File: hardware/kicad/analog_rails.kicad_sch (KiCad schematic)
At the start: 35 parts, among them U401 LMR62014XMF, U402 LT3042EMSE, U403 LM27761DSG, U404 REF5025AID

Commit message: feat(hardware)!: draw draft A1 of the schematic around a Pico 2
A Raspberry Pi Pico 2 on two 1x20 sockets replaces the ESP32-S3
development board, the programmable logic device and the buffer
between the two boards (D-39 to D-43 of the specification). The former
interface and range logic sheets become two new ones:

- Controller: the Pico 2, the diodes that join its USB supply and the
  5 V rail of the carrier, resistor arrays in the SPI and acquisition
  lines, a reset button and a console header.
- Side Data: two shift registers that take the range, the status
  signals and the eight logic inputs with every sample.

The DUT connects through a 1x4 pin header and a lever terminal block
in parallel, both GND, VIN, VOUT, GND, and the logic port is a 1x10
header with VCC, GND, D7 to D0: the pin order of the PPK2 (D-44). A
solder jumper selects the supply of the DUT side of the level
translator. A transistor at the driver of the ampere switch holds it
open while VIN is above 5.5 V.

Reference designators are numbered as the annotation tool of KiCad
does by default (D-45). The numbering touches every sheet, so these
changes come in one commit. The symbol and the socket footprint of
the ESP32-S3 board leave the project library; the Pico 2 uses the
symbol and the footprint of the KiCad library.

The electrical rules check reports no errors and no warnings. The
parts stay candidates, and no program for the PIO blocks exists yet.

BREAKING CHANGE: the pins of the controller follow the new pin map of
section 5 of the specification.
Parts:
- renumbered C402 to C10, C408 to C11, C409 to C12, C410 to C13, C411 to C14, C401 to C15, C403 to C16, C404 to C17, C405 to C18, C412 to C19, C407 to C20, C414 to C21, C413 to C22, C406 to C23, D401 to D5, L401 to L1, R410 to R10, R404 to R11, R405 to R12, R407 to R13, R406 to R14, R408 to R5, R401 to R6, R402 to R7, R403 to R8, R409 to R9, TP402 to TP10, TP403 to TP6, TP401 to TP7, TP405 to TP8, TP404 to TP9, U401 to U4, U403 to U5, U404 to U6, U402 to U7
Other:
- note added: "U4: VOUT = 1.23 V x (1 + R7 / R8) = 13.5 V, 1.6 MHz. U7: VOUT = 100 uA x R11 = 12.0 V; PG opens above 11 V (R12, R14). U5: VOUT = -1.22 V x (R9 + R10) / R10 = -3.98 V; R5 keeps VBUS transients off its 5.8 V rating. PWR_GOOD is pulled up to +3V3_C: with the carrier unpowered it reads low."
- note removed: "U401: VOUT = 1.23 V x (1 + R402 / R403) = 13.5 V, 1.6 MHz. U402: VOUT = 100 uA x R404 = 12.0 V; PG opens above 11 V (R405, R406). U403: VOUT = -1.22 V x (R409 + R410) / R410 = -3.98 V; R408 keeps VBUS transients off its 5.8 V rating. PWR_GOOD is pulled up to +3V3_C: with the carrier unpowered it reads low."

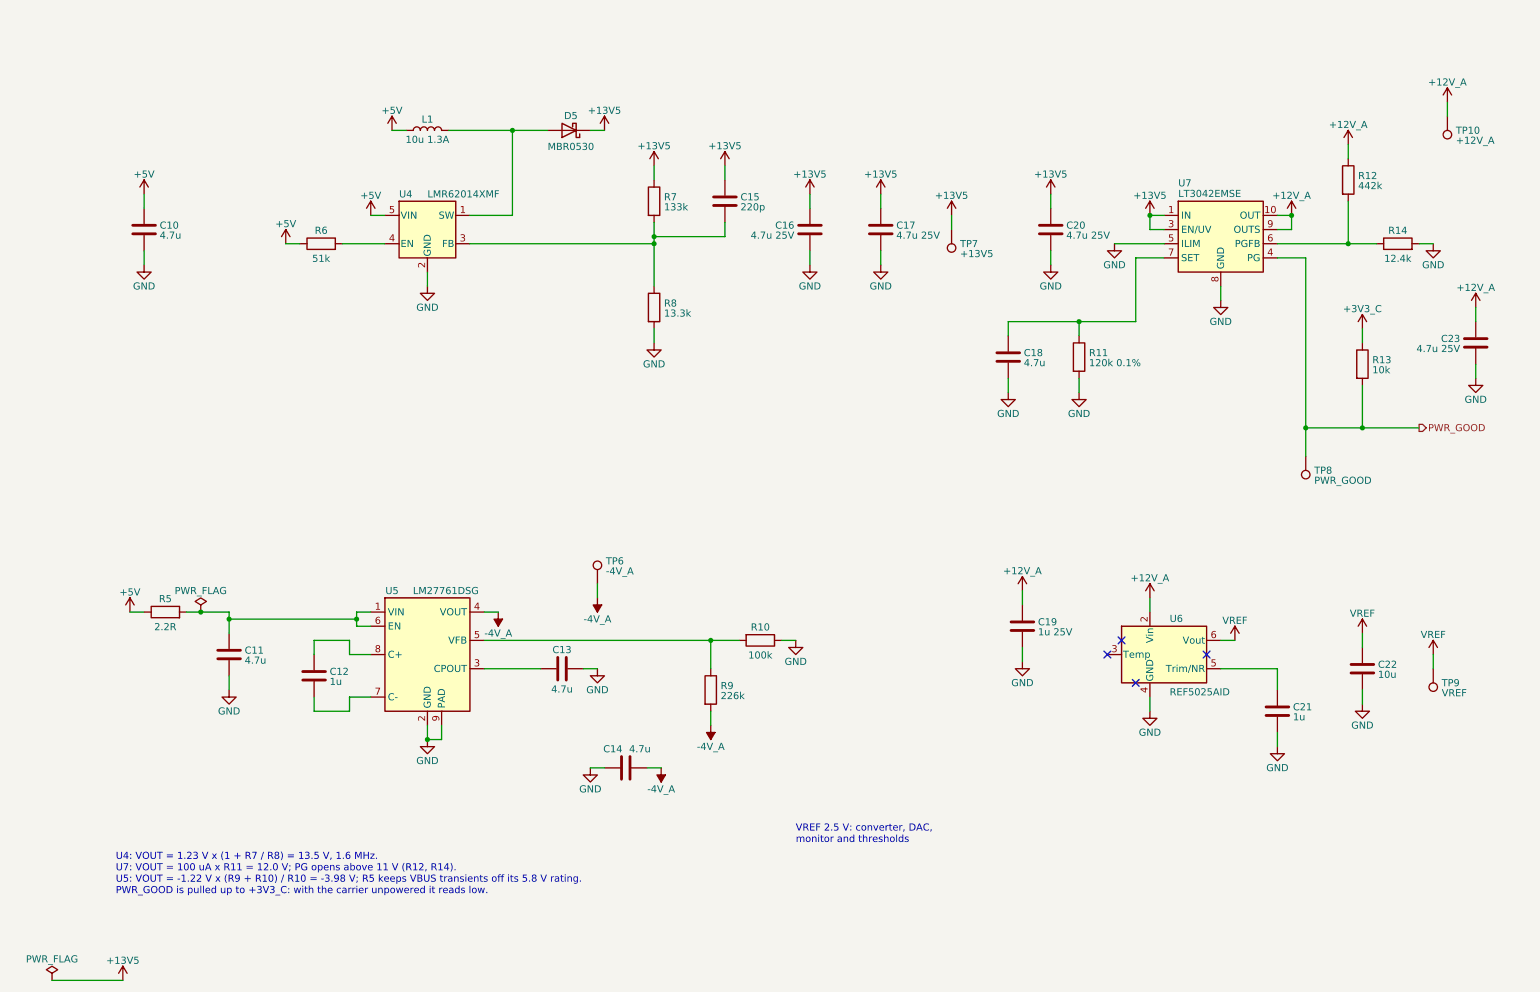
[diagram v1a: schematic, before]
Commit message: feat(hardware): draw draft A2 of the schematic
428 parts on 15 A4 pages, 14 sheets below the root sheet (D-83). Two
sheets are new: Logic Supplies, with the supervisor of the 5 V rail and
the two 3.3 V regulators, and Rail Monitor, with the comparators behind
PWR_GOOD.

The drawings follow the specification of draft A2: a current limiter
on each supply input and a priority multiplexer, a pre-regulator that
tracks the output of the linear regulator, a VIN path that withstands
-20 V to +20 V with its switch open, two diode-connected MOSFETs as
ladder clamp, thin-film and four-terminal shunts, ESD arrays at the CC
pins and at the VCC pin of the logic port. The reference designators
are numbered as KiCad numbers them (D-45), so they are not those of
draft A1.

The project library gains the symbol of the input multiplexer and two
footprints: the lever terminal block with pads of 1.9 mm x 2.3 mm and
the controller module without its antenna keep-out (D-85).

The electrical rules check reports no errors and no warnings. The
parts are candidates, and nothing is built or measured.
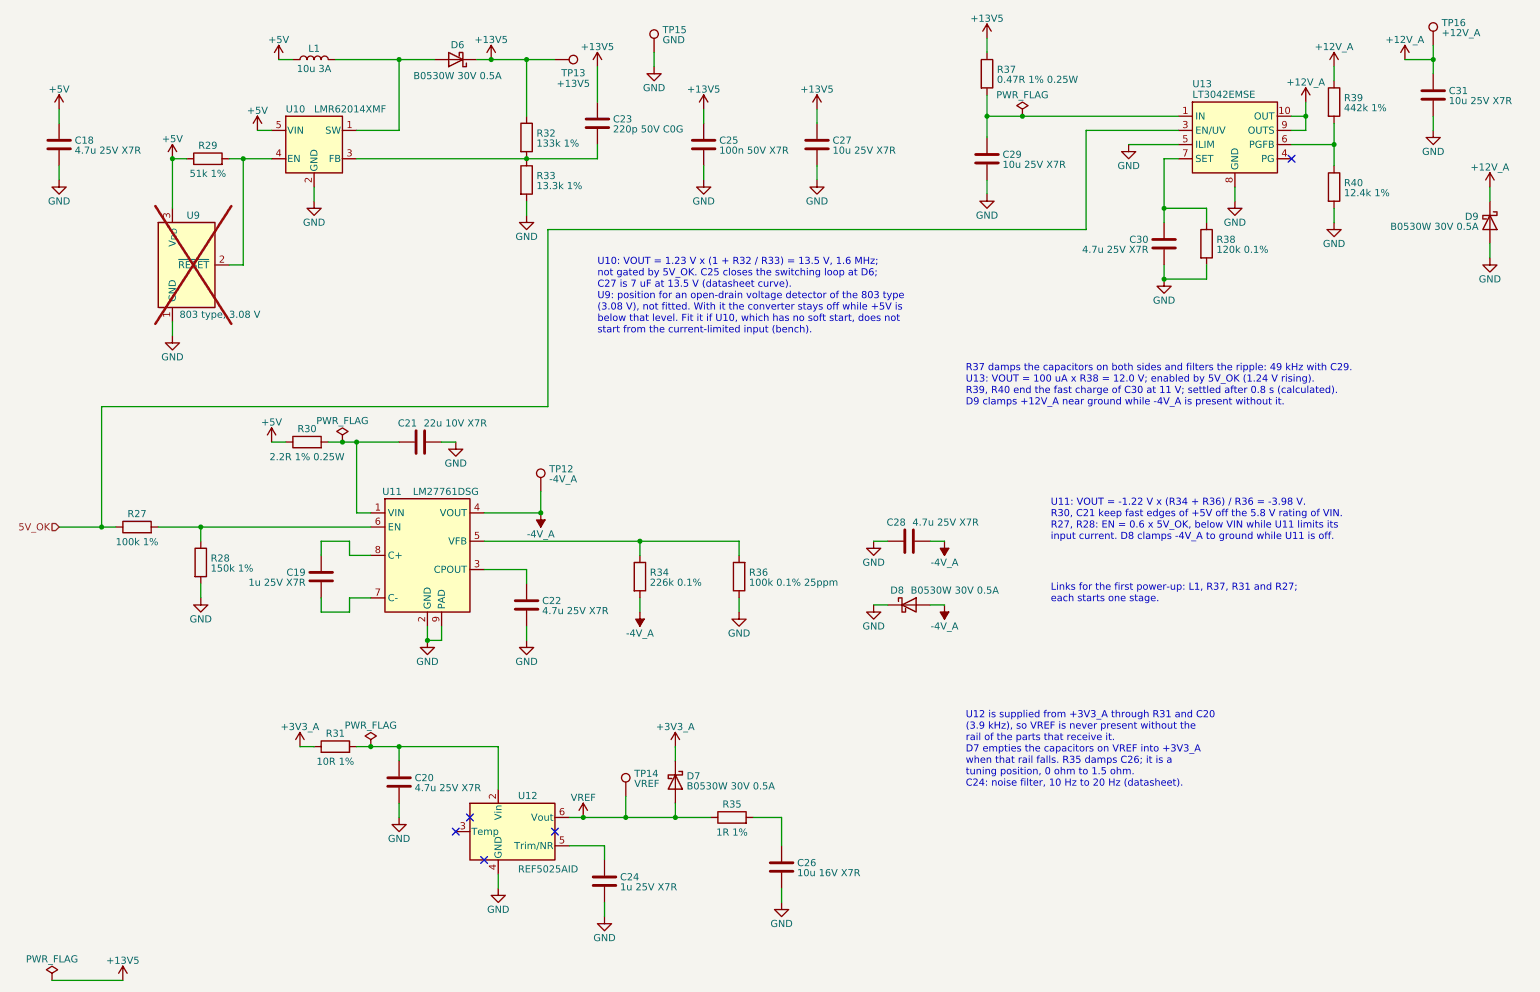
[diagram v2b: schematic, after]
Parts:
- removed R13: 10k, Resistor_SMD:R_0603_1608Metric, symbol Device:R
- removed TP8: PWR_GOOD, TestPoint:TestPoint_Pad_D1.5mm, symbol Connector:TestPoint
- added D7, D8, D9: B0530W 30V 0.5A, Diode_SMD:D_SOD-123, symbol Device:D_Schottky
- added R27: 100k 1%, Resistor_SMD:R_0603_1608Metric, symbol Device:R
- added R28: 150k 1%, Resistor_SMD:R_0603_1608Metric, symbol Device:R
- added R31: 10R 1%, Resistor_SMD:R_0603_1608Metric, symbol Device:R
- added R35: 1R 1%, Resistor_SMD:R_0603_1608Metric, symbol Device:R
- added R37: 0.47R 1% 0.25W, Resistor_SMD:R_1206_3216Metric, symbol Device:R
- added TP15: GND, TestPoint:TestPoint_Pad_2.0x2.0mm, symbol Connector:TestPoint
- added U9: 803 type, 3.08 V, Package_TO_SOT_SMD:SOT-23, symbol Power_Supervisor:TCM809
- C18: renamed from C10; value 4.7u -> 4.7u 25V X7R; MPN (none) -> CL21B475KAFNNNE; Manufacturer (none) -> Samsung Electro-Mechanics
- C19: renamed from C12; value 1u -> 1u 25V X7R; MPN (none) -> C0603C105K3RACTU; Manufacturer (none) -> KEMET
- C20: renamed from C19; value 1u 25V -> 4.7u 25V X7R; footprint Capacitor_SMD:C_0603_1608Metric -> Capacitor_SMD:C_0805_2012Metric; MPN (none) -> CL21B475KAFNNNE; Manufacturer (none) -> Samsung Electro-Mechanics
- C21: renamed from C11; value 4.7u -> 22u 10V X7R; footprint Capacitor_SMD:C_0805_2012Metric -> Capacitor_SMD:C_1206_3216Metric; MPN (none) -> CL31B226KPHNNNE; Manufacturer (none) -> Samsung Electro-Mechanics
- C22: renamed from C13; value 4.7u -> 4.7u 25V X7R; MPN (none) -> CL21B475KAFNNNE; Manufacturer (none) -> Samsung Electro-Mechanics
- C23: renamed from C15; value 220p -> 220p 50V C0G; MPN (none) -> C0603C221J5GACTU; Manufacturer (none) -> KEMET
- C24: renamed from C21; value 1u -> 1u 25V X7R; MPN (none) -> C0603C105K3RACTU; Manufacturer (none) -> KEMET
- C25: renamed from C17; value 4.7u 25V -> 100n 50V X7R; footprint Capacitor_SMD:C_0805_2012Metric -> Capacitor_SMD:C_0603_1608Metric; MPN (none) -> C0603C104K5RACTU; Manufacturer (none) -> KEMET
- C26: renamed from C22; value 10u -> 10u 16V X7R; MPN (none) -> CL21B106KOQNNNE; Manufacturer (none) -> Samsung Electro-Mechanics
- C27: renamed from C16; value 4.7u 25V -> 10u 25V X7R; footprint Capacitor_SMD:C_0805_2012Metric -> Capacitor_SMD:C_1210_3225Metric; MPN (none) -> CL32B106KAJNNNE; Manufacturer (none) -> Samsung Electro-Mechanics
- C28: renamed from C14; value 4.7u -> 4.7u 25V X7R; MPN (none) -> CL21B475KAFNNNE; Manufacturer (none) -> Samsung Electro-Mechanics
- C29: renamed from C20; value 4.7u 25V -> 10u 25V X7R; footprint Capacitor_SMD:C_0805_2012Metric -> Capacitor_SMD:C_1210_3225Metric; MPN (none) -> CL32B106KAJNNNE; Manufacturer (none) -> Samsung Electro-Mechanics
- C30: renamed from C18; value 4.7u -> 4.7u 25V X7R; MPN (none) -> CL21B475KAFNNNE; Manufacturer (none) -> Samsung Electro-Mechanics
- C31: renamed from C23; value 4.7u 25V -> 10u 25V X7R; footprint Capacitor_SMD:C_0805_2012Metric -> Capacitor_SMD:C_1210_3225Metric; MPN (none) -> CL32B106KAJNNNE; Manufacturer (none) -> Samsung Electro-Mechanics
- D6: renamed from D5; value MBR0530 -> B0530W 30V 0.5A; MPN (none) -> B0530W-7-F; Manufacturer (none) -> Diodes Incorporated
- L1: value 10u 1.3A -> 10u 3A; footprint Inductor_SMD:L_Changjiang_FNR4020S -> Inductor_SMD:L_Wuerth_MAPI-4030; MPN FNR4020S100MT -> 74438357100; Manufacturer (none) -> Wurth Elektronik
- R29: renamed from R6; value 51k -> 51k 1%; MPN (none) -> CRCW060351K0FKEA; Manufacturer (none) -> Vishay
- R30: renamed from R5; value 2.2R -> 2.2R 1% 0.25W; footprint Resistor_SMD:R_0603_1608Metric -> Resistor_SMD:R_1206_3216Metric; MPN (none) -> CRCW12062R20FKEA; Manufacturer (none) -> Vishay
- R32: renamed from R7; value 133k -> 133k 1%; MPN (none) -> CRCW0603133KFKEA; Manufacturer (none) -> Vishay
- R33: renamed from R8; value 13.3k -> 13.3k 1%; MPN (none) -> CRCW060313K3FKEA; Manufacturer (none) -> Vishay
- R34: renamed from R9; value 226k -> 226k 0.1%; MPN (none) -> TNPW0603226KBEEA; Manufacturer (none) -> Vishay
- R36: renamed from R10; value 100k -> 100k 0.1% 25ppm; MPN (none) -> TNPW0603100KBEEA; Manufacturer (none) -> Vishay
- R38: renamed from R11; MPN (none) -> TNPW0603120KBEEA; Manufacturer (none) -> Vishay
- R39: renamed from R12; value 442k -> 442k 1%; MPN (none) -> CRCW0603442KFKEA; Manufacturer (none) -> Vishay
- R40: renamed from R14; value 12.4k -> 12.4k 1%; MPN (none) -> CRCW060312K4FKEA; Manufacturer (none) -> Vishay
- TP12: renamed from TP6; now left out of the parts list
- TP13: renamed from TP7; now left out of the parts list
- TP14: renamed from TP9; now left out of the parts list
- TP16: renamed from TP10; now left out of the parts list
- U10: renamed from U4; MPN (none) -> LMR62014XMF/NOPB; Manufacturer (none) -> Texas Instruments
- U11: renamed from U5; MPN (none) -> LM27761DSGT; Manufacturer (none) -> Texas Instruments
- U12: renamed from U6; MPN (none) -> REF5025AID; Manufacturer (none) -> Texas Instruments
- U13: renamed from U7; MPN (none) -> LT3042EMSE#PBF; Manufacturer (none) -> Analog Devices
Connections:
- net +12V_A: now also D9.1 (K); no longer C20.1, U12.2 (Vin)
- net +13V5: now also R37.1; no longer C29.1, U13.1 (IN), U13.2 (IN), U13.3 (EN/UV)
- net +5V: now also U9.3 (V_{DD})
- net -4V_A: now also D8.2 (A)
- net GND: now also D8.1 (K), D9.2 (A), R28.2, TP15.1, U9.1 (GND)
- net VREF: now also D7.2 (A), R35.1; no longer C26.1
- net at C21.1, R30.2, U11.1 (VIN): no longer U11.6 (EN)
- net at R29.2, U10.4 (EN): now also U9.2 (~{RESET})
- net PWR_GOOD: no longer names the net of U13.4 (PG)
- new net: C20.1, R31.2, U12.2 (Vin)
- new net: C26.1, R35.2
- new net: C29.1, R37.2, U13.1 (IN), U13.2 (IN)
- new net: R27.2, R28.1, U11.6 (EN)
- new net +3V3_A: D7.1 (K), R31.1
- new net 5V_OK: R27.1, U13.3 (EN/UV)
- no-connect marks 4 -> 5
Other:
- note added: "Links for the first power-up: L1, R37, R31 and R27; each starts one stage."
- note added: "R37 damps the capacitors on both sides and filters the ripple: 49 kHz with C29. U13: VOUT = 100 uA x R38 = 12.0 V; enabled by 5V_OK (1.24 V rising). R39, R40 end the fast charge of C30 at 11 V; settled after 0.8 s (calculated). D9 clamps +12V_A near ground while -4V_A is present without it."
- note added: "U10: VOUT = 1.23 V x (1 + R32 / R33) = 13.5 V, 1.6 MHz; not gated by 5V_OK. C25 closes the switching loop at D6; C27 is 7 uF at 13.5 V (datasheet curve). U9: position for an open-drain voltage detector of the 803 type (3.08 V), not fitted. With it the converter stays off while +5V is below that level. Fit it if U10, which has no soft start, does not start from the current-limited input (bench)."
- note added: "U11: VOUT = -1.22 V x (R34 + R36) / R36 = -3.98 V. R30, C21 keep fast edges of +5V off the 5.8 V rating of VIN. R27, R28: EN = 0.6 x 5V_OK, below VIN while U11 limits its input current. D8 clamps -4V_A to ground while U11 is off."
- note added: "U12 is supplied from +3V3_A through R31 and C20 (3.9 kHz), so VREF is never present without the rail of the parts that receive it. D7 empties the capacitors on VREF into +3V3_A when that rail falls. R35 damps C26; it is a tuning position, 0 ohm to 1.5 ohm. C24: noise filter, 10 Hz to 20 Hz (datasheet)."
- note removed: "U4: VOUT = 1.23 V x (1 + R7 / R8) = 13.5 V, 1.6 MHz. U7: VOUT = 100 uA x R11 = 12.0 V; PG opens above 11 V (R12, R14). U5: VOUT = -1.22 V x (R9 + R10) / R10 = -3.98 V; R5 keeps VBUS transients off its 5.8 V rating. PWR_GOOD is pulled up to +3V3_C: with the carrier unpowered it reads low."
- note removed: "VREF 2.5 V: converter, DAC, monitor and thresholds"
- moved on the sheet: C18, C19, C20, C21, C22, C23, C24, C25, C26, C27, C28, C29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
